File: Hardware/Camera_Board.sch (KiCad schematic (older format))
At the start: 15 parts, among them J4 Camera_Right, J5 Camera_Left, J6 Motherboard_Right, J7 Motherboard_Left

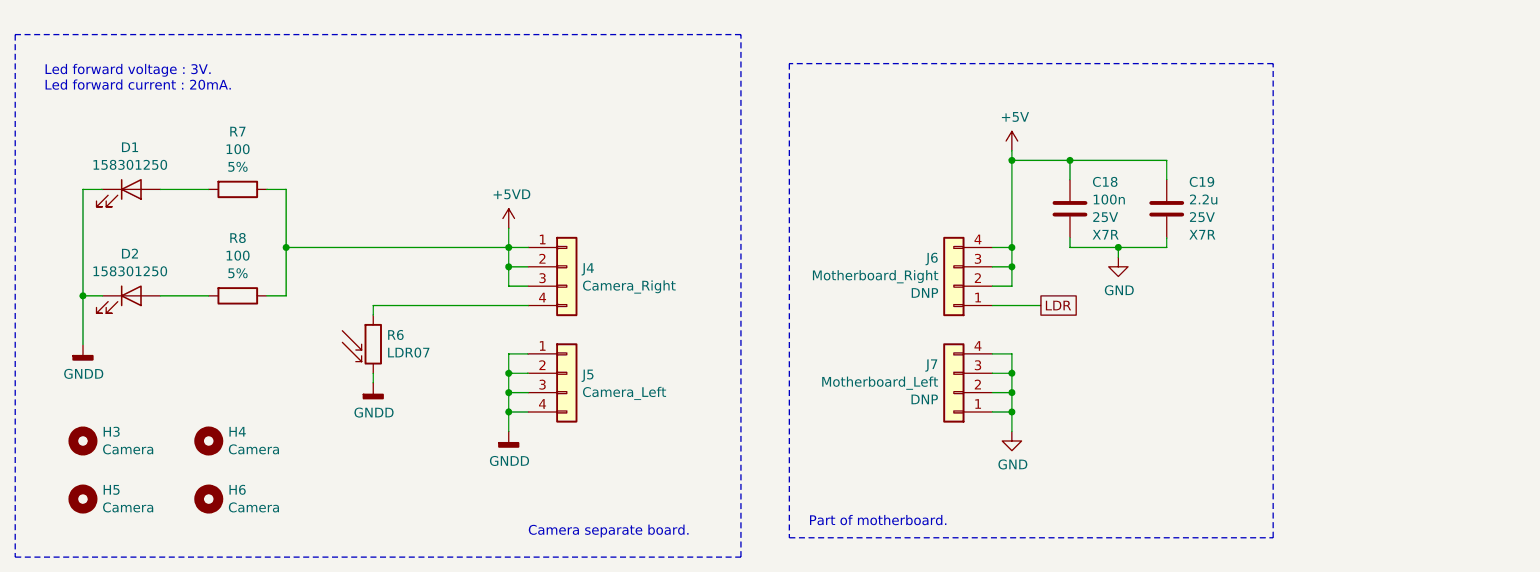
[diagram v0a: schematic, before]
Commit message: [Hardware] Added a transistor to enable leds control from Raspberry Pi.
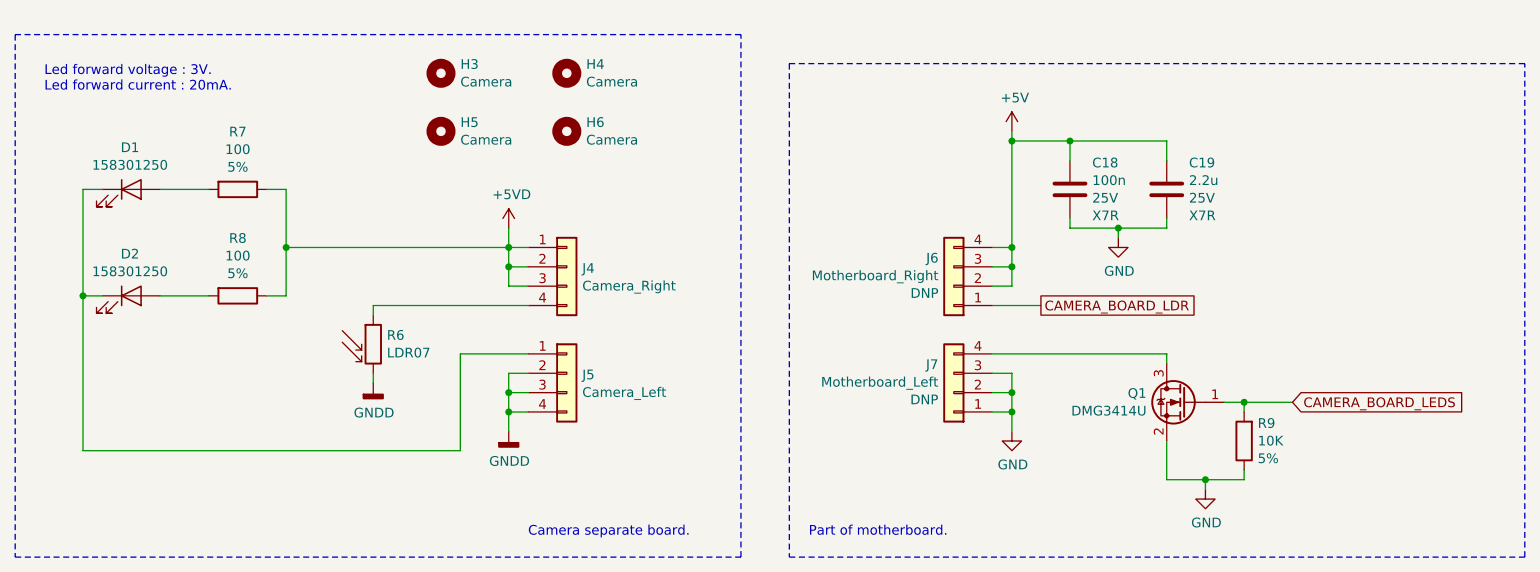
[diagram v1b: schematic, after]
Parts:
- added Q1: DMG3414U, Package_TO_SOT_SMD:SOT-23, symbol Transistor_FET:DMG3414U
- added R9: 10K, Resistor_SMD:R_1206_3216Metric_Pad1.42x1.75mm_HandSolder, symbol Device:R
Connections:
- net GND: now also Q1.2 (S), R9.1; no longer J7.4 (Pin_4)
- net GNDD: no longer D1.1 (K), D2.1 (K), J5.1 (Pin_1)
- net LDR renamed CAMERA_BOARD_LDR
- new net: D1.1 (K), D2.1 (K), J5.1 (Pin_1)
- new net: J7.4 (Pin_4), Q1.3 (D)
- new net CAMERA_BOARD_LEDS: Q1.1 (G), R9.2
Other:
- moved on the sheet: C18, C19, H3, H4, H5, H6
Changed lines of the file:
@@
 	7650 4300 7650 4400
 Connection ~ 7650 4400
-Wire Wire Line
-	7550 4200 7650 4200
-Wire Wire Line
-	7650 4200 7650 4300
-Connection ~ 7650 4300
 $Comp
 L power:GNDD #PWR0102
@@
 	5050 4300 5050 4400
 Connection ~ 5050 4400
-Wire Wire Line
-	5150 4200 5050 4200
-Wire Wire Line
-	5050 4200 5050 4300
-Connection ~ 5050 4300
 $Comp
 L power:+5V #PWR0103
 U 1 1 5F2A1CD1
-P 7650 3150
-F 0 "#PWR0103" H 7650 3000 50  0001 C CNN
-F 1 "+5V" H 7665 3323 50  0000 C CNN
-F 2 "" H 7650 3150 50  0001 C CNN
-F 3 "" H 7650 3150 50  0001 C CNN
-	1    7650 3150
+P 7650 3050
+F 0 "#PWR0103" H 7650 2900 50  0001 C CNN
+F 1 "+5V" H 7665 3223 50  0000 C CNN
+F 2 "" H 7650 3050 50  0001 C CNN
+F 3 "" H 7650 3050 50  0001 C CNN
+	1    7650 3050
 	1    0    0    -1
 $EndComp
@@
 L Device:C C?
 U 1 1 5F2A61A6
-P 7950 3450
+P 7950 3350
 AR Path="/5F1F2F9E/5F2A61A6" Ref="C?"  Part="1"
 AR Path="/5F22814A/5F2A61A6" Ref="C?"  Part="1"
 AR Path="/5F288D93/5F2A61A6" Ref="C18"  Part="1"
-F 0 "C18" H 7835 3313 50  0000 R CNN
-F 1 "100n" H 7835 3404 50  0000 R CNN
-F 2 "Capacitor_SMD:C_1206_3216Metric_Pad1.42x1.75mm_HandSolder" H 7988 3300 50  0001 C CNN
-F 3 "~" H 7950 3450 50  0001 C CNN
-F 4 "25V" H 7835 3495 50  0000 R CNN "Value2"
-F 5 "X7R" H 7835 3586 50  0000 R CNN "Value3"
-	1    7950 3450
+F 0 "C18" H 7835 3213 50  0000 R CNN
+F 1 "100n" H 7835 3304 50  0000 R CNN
+F 2 "Capacitor_SMD:C_1206_3216Metric_Pad1.42x1.75mm_HandSolder" H 7988 3200 50  0001 C CNN
+F 3 "~" H 7950 3350 50  0001 C CNN
+F 4 "25V" H 7835 3395 50  0000 R CNN "Value2"
+F 5 "X7R" H 7835 3486 50  0000 R CNN "Value3"
+	1    7950 3350
 	-1   0    0    1
 $EndComp
@@
 L Device:C C?
 U 1 1 5F2A61AE
-P 8450 3450
+P 8450 3350
 AR Path="/5F1F2F9E/5F2A61AE" Ref="C?"  Part="1"
 AR Path="/5F22814A/5F2A61AE" Ref="C?"  Part="1"
 AR Path="/5F288D93/5F2A61AE" Ref="C19"  Part="1"
-F 0 "C19" H 8335 3313 50  0000 R CNN
-F 1 "2.2u" H 8335 3404 50  0000 R CNN
-F 2 "Capacitor_SMD:C_1206_3216Metric_Pad1.42x1.75mm_HandSolder" H 8488 3300 50  0001 C CNN
-F 3 "~" H 8450 3450 50  0001 C CNN
-F 4 "25V" H 8335 3495 50  0000 R CNN "Value2"
-F 5 "X7R" H 8335 3586 50  0000 R CNN "Value3"
-	1    8450 3450
+F 0 "C19" H 8335 3213 50  0000 R CNN
+F 1 "2.2u" H 8335 3304 50  0000 R CNN
+F 2 "Capacitor_SMD:C_1206_3216Metric_Pad1.42x1.75mm_HandSolder" H 8488 3200 50  0001 C CNN
+F 3 "~" H 8450 3350 50  0001 C CNN
+F 4 "25V" H 8335 3395 50  0000 R CNN "Value2"
+F 5 "X7R" H 8335 3486 50  0000 R CNN "Value3"
+	1    8450 3350
 	-1   0    0    1
 $EndComp
 Wire Wire Line
-	7650 3200 7950 3200
-Wire Wire Line
-	7950 3200 7950 3300
-Wire Wire Line
-	7950 3200 8450 3200
-Wire Wire Line
-	8450 3200 8450 3300
-Connection ~ 7950 3200
-Wire Wire Line
-	7950 3600 7950 3650
-Wire Wire Line
-	8450 3650 8450 3600
-Wire Wire Line
-	7950 3650 8200 3650
+	7650 3100 7950 3100
+Wire Wire Line
+	7950 3100 7950 3200
+Wire Wire Line
+	7950 3100 8450 3100
+Wire Wire Line
+	8450 3100 8450 3200
+Connection ~ 7950 3100
+Wire Wire Line
+	7950 3500 7950 3550
+Wire Wire Line
+	8450 3550 8450 3500
+Wire Wire Line
+	7950 3550 8200 3550
 $Comp
 L power:GND #PWR0104
 U 1 1 5F2AC559
-P 8200 3700
-F 0 "#PWR0104" H 8200 3450 50  0001 C CNN
-F 1 "GND" H 8205 3527 50  0000 C CNN
-F 2 "" H 8200 3700 50  0001 C CNN
-F 3 "" H 8200 3700 50  0001 C CNN
-	1    8200 3700
-	1    0    0    -1
-$EndComp
-Wire Wire Line
-	8200 3700 8200 3650
-Connection ~ 8200 3650
-Wire Wire Line
-	8200 3650 8450 3650
-Wire Wire Line
-	7650 3150 7650 3200
-Wire Wire Line
-	7650 3200 7650 3650
-Connection ~ 7650 3200
+P 8200 3600
+F 0 "#PWR0104" H 8200 3350 50  0001 C CNN
+F 1 "GND" H 8205 3427 50  0000 C CNN
+F 2 "" H 8200 3600 50  0001 C CNN
+F 3 "" H 8200 3600 50  0001 C CNN
+	1    8200 3600
+	1    0    0    -1
+$EndComp
+Wire Wire Line
+	8200 3600 8200 3550
+Connection ~ 8200 3550
+Wire Wire Line
+	8200 3550 8450 3550
 Text GLabel 7800 3950 2    50   UnSpc ~ 0
-LDR
+CAMERA_BOARD_LDR
 Wire Wire Line
 	7800 3950 7550 3950
 Wire Notes Line
-	6500 5150 9000 5150
-Wire Notes Line
-	9000 5150 9000 2700
-Wire Notes Line
-	9000 2700 6500 2700
-Wire Notes Line
-	6500 2700 6500 5150
-Text Notes 6600 5100 0    50   ~ 0
+	6500 5250 10300 5250
+Wire Notes Line
+	10300 5250 10300 2700
+Wire Notes Line
+	10300 2700 6500 2700
+Wire Notes Line
+	6500 2700 6500 5250
+Text Notes 6600 5150 0    50   ~ 0
 Part of motherboard.
 $Comp
@@
 Wire Wire Line
 	4350 3950 4350 4000
-$Comp
-L power:GNDD #PWR0107
-U 1 1 5F2C704C
-P 2850 4150
-F 0 "#PWR0107" H 2850 3900 50  0001 C CNN
-F 1 "GNDD" H 2854 3995 50  0000 C CNN
-F 2 "" H 2850 4150 50  0001 C CNN
-F 3 "" H 2850 4150 50  0001 C CNN
-	1    2850 4150
-	1    0    0    -1
-$EndComp
 Wire Wire Line
 	2950 3900 2850 3900
 Wire Wire Line
-	2850 3900 2850 4150
-Wire Wire Line
 	2850 3900 2850 3350
 Wire Wire Line
 	2850 3350 2950 3350
-Connection ~ 2850 3900
 Text Notes 2650 2850 0    50   ~ 0
 Led forward voltage : 3V.\nLed forward current : 20mA.
@@
 L Mechanical:MountingHole H3
 U 1 1 5F2EC62F
-P 2850 4650
-F 0 "H3" H 2950 4696 50  0000 L CNN
-F 1 "Camera" H 2950 4605 50  0000 L CNN
-F 2 "MountingHole:MountingHole_2.2mm_M2" H 2850 4650 50  0001 C CNN
-F 3 "~" H 2850 4650 50  0001 C CNN
-	1    2850 4650
+P 4700 2750
+F 0 "H3" H 4800 2796 50  0000 L CNN
+F 1 "Camera" H 4800 2705 50  0000 L CNN
+F 2 "MountingHole:MountingHole_2.2mm_M2" H 4700 2750 50  0001 C CNN
+F 3 "~" H 4700 2750 50  0001 C CNN
+	1    4700 2750
 	1    0    0    -1
 $EndComp
@@
 L Mechanical:MountingHole H4
 U 1 1 5F2F030A
-P 3500 4650
-F 0 "H4" H 3600 4696 50  0000 L CNN
-F 1 "Camera" H 3600 4605 50  0000 L CNN
-F 2 "MountingHole:MountingHole_2.2mm_M2" H 3500 4650 50  0001 C CNN
-F 3 "~" H 3500 4650 50  0001 C CNN
-	1    3500 4650
+P 5350 2750
+F 0 "H4" H 5450 2796 50  0000 L CNN
+F 1 "Camera" H 5450 2705 50  0000 L CNN
+F 2 "MountingHole:MountingHole_2.2mm_M2" H 5350 2750 50  0001 C CNN
+F 3 "~" H 5350 2750 50  0001 C CNN
+	1    5350 2750
 	1    0    0    -1
 $EndComp
@@
 L Mechanical:MountingHole H5
 U 1 1 5F2F0621
-P 2850 4950
-F 0 "H5" H 2950 4996 50  0000 L CNN
-F 1 "Camera" H 2950 4905 50  0000 L CNN
-F 2 "MountingHole:MountingHole_2.2mm_M2" H 2850 4950 50  0001 C CNN
-F 3 "~" H 2850 4950 50  0001 C CNN
-	1    2850 4950
+P 4700 3050
+F 0 "H5" H 4800 3096 50  0000 L CNN
+F 1 "Camera" H 4800 3005 50  0000 L CNN
+F 2 "MountingHole:MountingHole_2.2mm_M2" H 4700 3050 50  0001 C CNN
+F 3 "~" H 4700 3050 50  0001 C CNN
+	1    4700 3050
 	1    0    0    -1
 $EndComp
@@
 L Mechanical:MountingHole H6
 U 1 1 5F2F098F
-P 3500 4950
-F 0 "H6" H 3600 4996 50  0000 L CNN
-F 1 "Camera" H 3600 4905 50  0000 L CNN
-F 2 "MountingHole:MountingHole_2.2mm_M2" H 3500 4950 50  0001 C CNN
-F 3 "~" H 3500 4950 50  0001 C CNN
-	1    3500 4950
+P 5350 3050
+F 0 "H6" H 5450 3096 50  0000 L CNN
+F 1 "Camera" H 5450 3005 50  0000 L CNN
+F 2 "MountingHole:MountingHole_2.2mm_M2" H 5350 3050 50  0001 C CNN
+F 3 "~" H 5350 3050 50  0001 C CNN
+	1    5350 3050
 	1    0    0    -1
 $EndComp
@@
 Text Notes 5150 5150 0    50   ~ 0
 Camera separate board.
+Wire Wire Line
+	5150 4200 4800 4200
+Wire Wire Line
+	4800 4200 4800 4700
+Wire Wire Line
+	4800 4700 2850 4700
+Wire Wire Line
+	2850 4700 2850 3900
+Connection ~ 2850 3900
+$Comp
+L Transistor_FET:DMG3414U Q1
+U 1 1 5F310BD3
+P 8550 4450
+F 0 "Q1" H 8754 4496 50  0000 L CNN
+F 1 "DMG3414U" H 8754 4405 50  0000 L CNN
+F 2 "Package_TO_SOT_SMD:SOT-23" H 8750 4375 50  0001 L CIN
+F 3 "http://www.diodes.com/assets/Datasheets/ds31739.pdf" H 8550 4450 50  0001 L CNN
+	1    8550 4450
+	-1   0    0    -1
+$EndComp
+$Comp
+L power:GND #PWR013
+U 1 1 5F3169A9
+P 8650 4900
+F 0 "#PWR013" H 8650 4650 50  0001 C CNN
+F 1 "GND" H 8655 4727 50  0000 C CNN
+F 2 "" H 8650 4900 50  0001 C CNN
+F 3 "" H 8650 4900 50  0001 C CNN
+	1    8650 4900
+	1    0    0    -1
+$EndComp
+Wire Wire Line
+	8450 4200 8450 4250
+Wire Wire Line
+	7550 4200 8450 4200
+$Comp
+L Device:R R9
+U 1 1 5F31C7BD
+P 8850 4650
+F 0 "R9" H 8780 4559 50  0000 R CNN
+F 1 "10K" H 8780 4650 50  0000 R CNN
+F 2 "Resistor_SMD:R_1206_3216Metric_Pad1.42x1.75mm_HandSolder" V 8780 4650 50  0001 C CNN
+F 3 "~" H 8850 4650 50  0001 C CNN
+F 4 "5%" H 8780 4741 50  0000 R CNN "Value2"
+	1    8850 4650
+	-1   0    0    1
+$EndComp
+Wire Wire Line
+	8450 4850 8650 4850
+Wire Wire Line
+	8650 4850 8650 4900
+Wire Wire Line
+	8450 4650 8450 4850
+Wire Wire Line
+	8650 4850 8850 4850
+Wire Wire Line
+	8850 4850 8850 4800
+Connection ~ 8650 4850
+Wire Wire Line
+	8750 4450 8850 4450
+Wire Wire Line
+	8850 4450 8850 4500
+Text GLabel 9100 4450 2    50   Input ~ 0
+CAMERA_BOARD_LEDS
+Wire Wire Line
+	8850 4450 9100 4450
+Connection ~ 8850 4450
+Wire Wire Line
+	7650 3050 7650 3100
+Connection ~ 7650 3100
+Wire Wire Line
+	7650 3100 7650 3650
 $EndSCHEMATC

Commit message: [Hardware] Removed the multiple connectors that were holding the front board, they will be replaced by angle brackets.
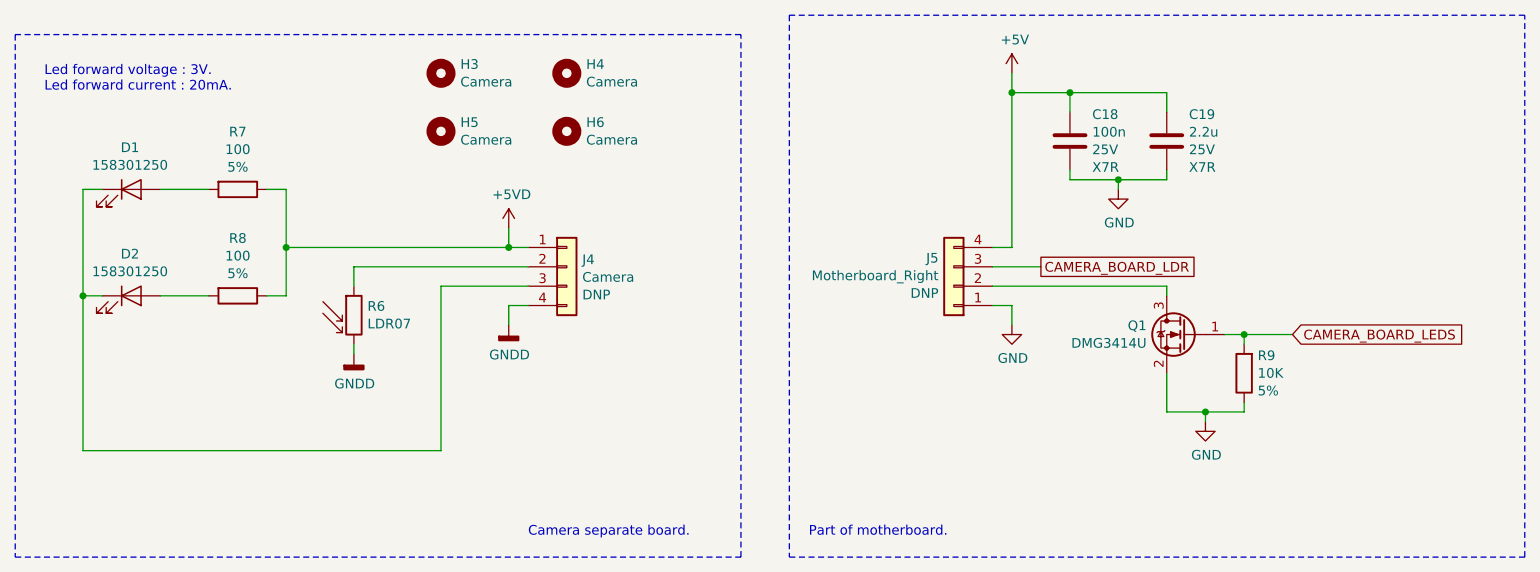
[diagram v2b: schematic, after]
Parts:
- removed J5: Camera_Left, Connector_PinHeader_2.54mm:PinHeader_1x04_P2.54mm_Horizontal, symbol Connector_Generic:Conn_01x04
- removed J7: Motherboard_Left, Connector_PinSocket_2.54mm:PinSocket_1x04_P2.54mm_Vertical, symbol Connector_Generic:Conn_01x04
- J4: value Camera_Right -> Camera; footprint Connector_PinHeader_2.54mm:PinHeader_1x04_P2.54mm_Horizontal -> Connector_PinHeader_2.54mm:PinHeader_1x04_P2.54mm_Vertical; Populate (none) -> DNP
- renumbered J6 to J5
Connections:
- net +5V: no longer J5.2 (Pin_2), J5.3 (Pin_3)
- net +5VD: no longer J4.2 (Pin_2), J4.3 (Pin_3)
- net CAMERA_BOARD_LDR: now also J5.3 (Pin_3); no longer J5.1 (Pin_1)
- net GND: now also J5.1 (Pin_1)
- net GNDD: now also J4.4 (Pin_4)
- net at D1.1 (K), D2.1 (K): now also J4.3 (Pin_3)
- net at R6.1: now also J4.2 (Pin_2); no longer J4.4 (Pin_4)
- net at Q1.3 (D): now also J5.2 (Pin_2)
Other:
- moved on the sheet: C18, C19, Q1, R6, R9
